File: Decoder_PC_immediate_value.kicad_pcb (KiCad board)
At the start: 4 copper layers, 66.4 x 62.6 mm, 10 parts

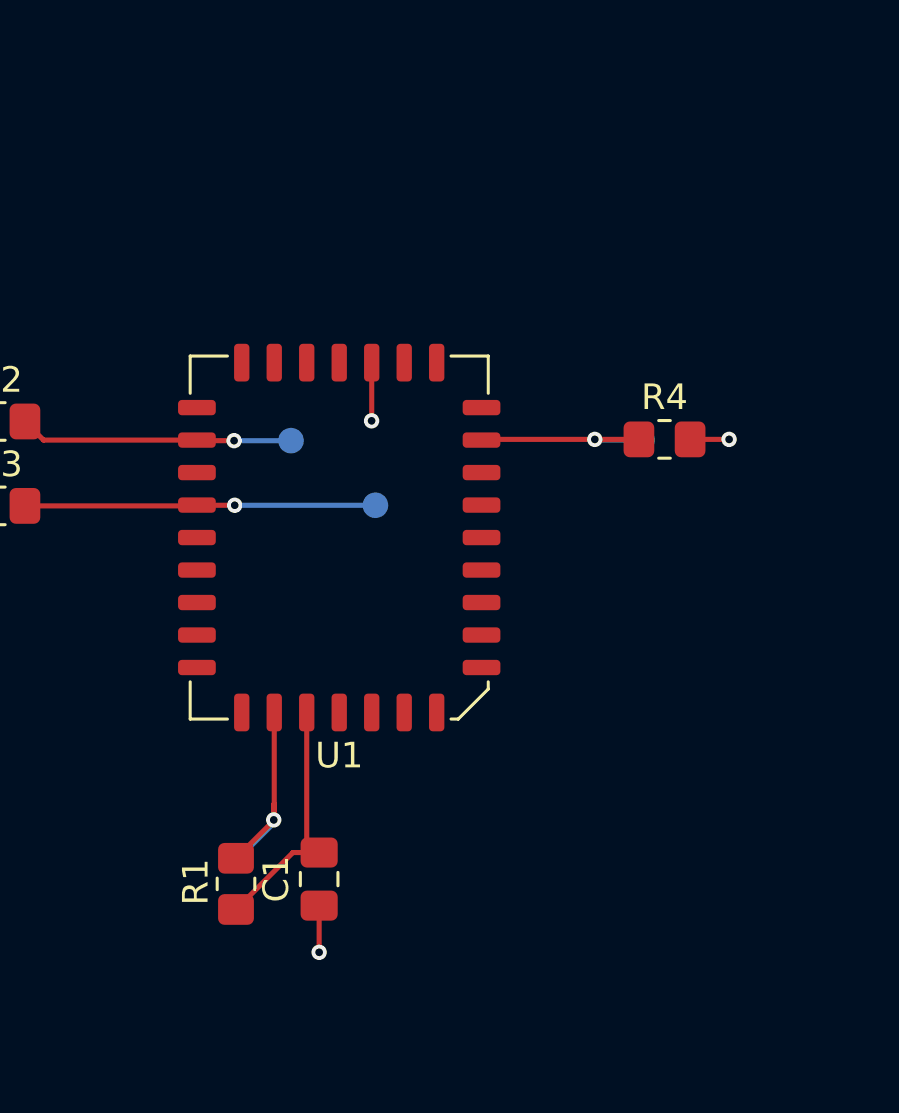
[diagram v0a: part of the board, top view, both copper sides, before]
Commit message: Added Output for Control Byte
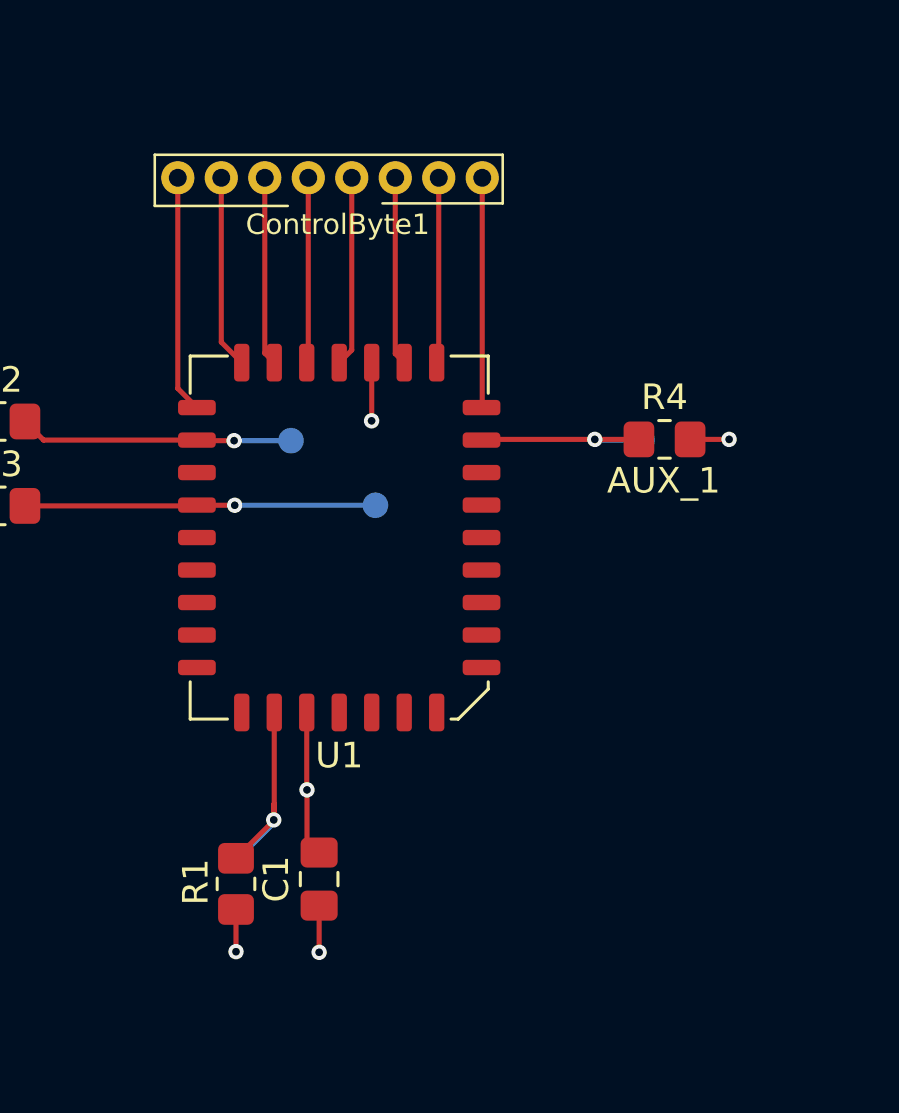
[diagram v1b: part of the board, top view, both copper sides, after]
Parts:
- added ControlByte1: ~, Other:8 Bit Bus Small, F.Cu at (94.5, 61.1)
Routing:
- net ControlWord7: track 0.00 -> 9.29 mm
- net ControlWord0: track 0.00 -> 8.99 mm
- net ControlWord6: track 0.00 -> 7.56 mm
- net ControlWord3: track 0.00 -> 7.43 mm
- net ControlWord5: track 0.00 -> 7.38 mm
- net ControlWord2: track 0.00 -> 7.37 mm
- net ControlWord1: track 0.00 -> 7.26 mm
- net ControlWord4: track 0.00 -> 7.25 mm
- net VCC: track 9.85 -> 8.01 mm, vias 0 -> 2
- added copper zone on In1.Cu, net VCC
- removed copper zone on In1.Cu, net (none)
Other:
- board text added: "AUX_1"

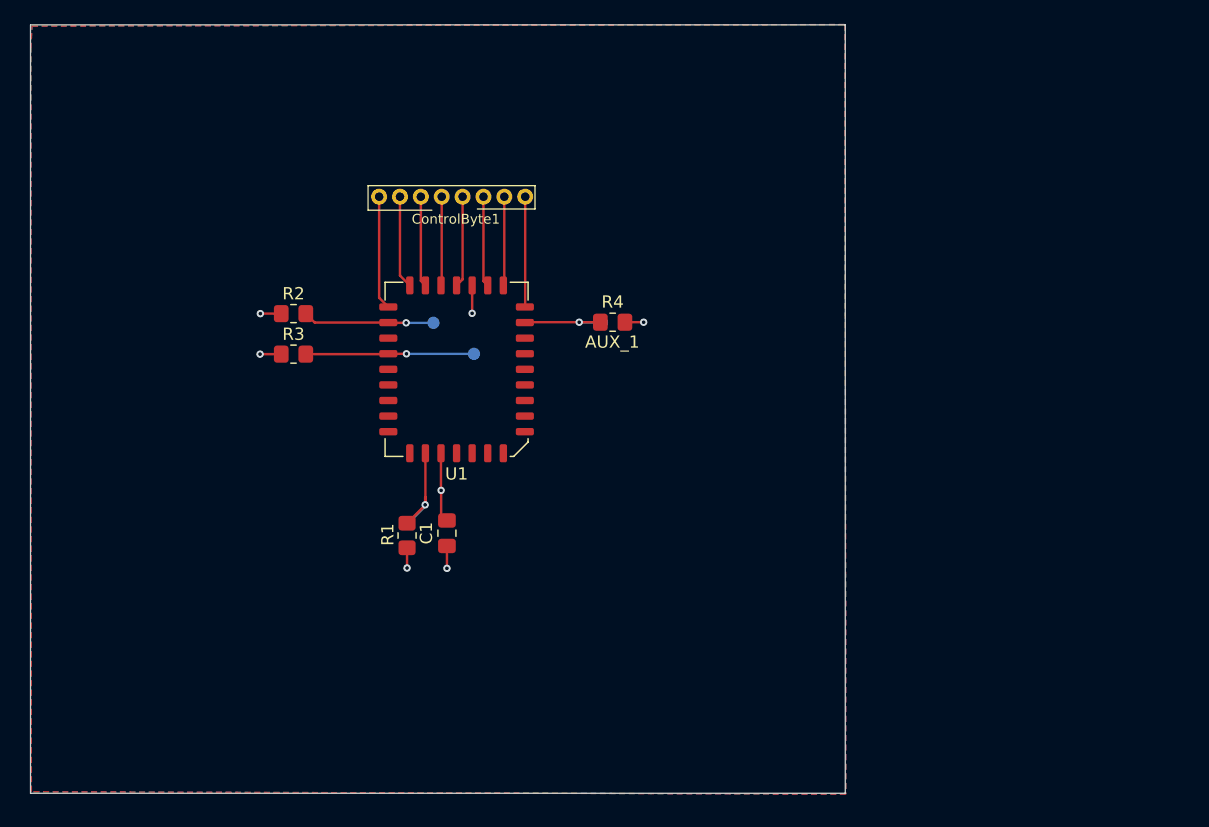
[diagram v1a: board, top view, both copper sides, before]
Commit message: Added Inputs for OP-Code
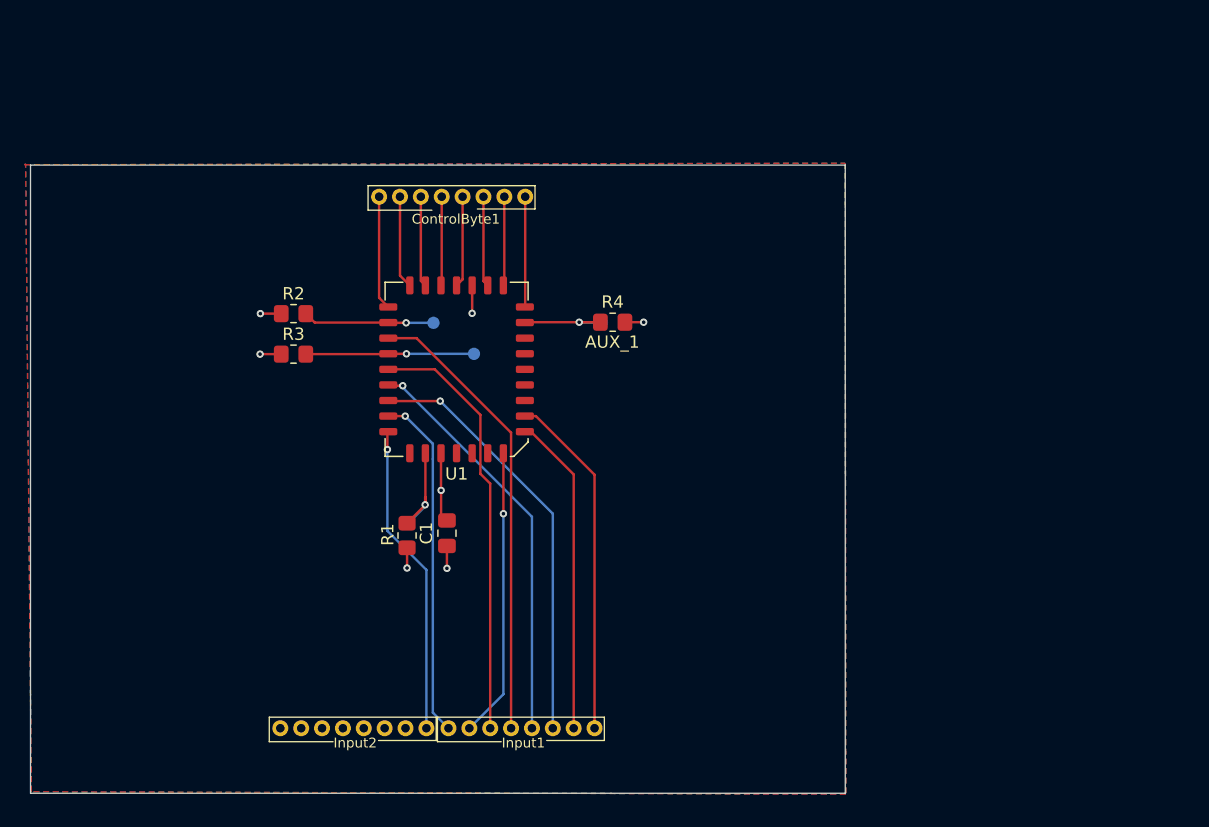
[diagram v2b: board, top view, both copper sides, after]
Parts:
- added Input1: ~, Other:8 Bit Bus Small, F.Cu at (100.2, 104.4)
- added Input2: ~, Other:8 Bit Bus Small, F.Cu at (86.5, 104.4)
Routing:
- net OP_Code_5: track 0.00 -> 37.3 mm
- net OP_Code_6: track 0.00 -> 34.9 mm
- net OP_Code_3: track 0.00 -> 34.7 mm, vias 0 -> 1
- net OP_Code_4: track 0.00 -> 33.5 mm, vias 0 -> 1
- net OP_Code_1: track 0.00 -> 28.3 mm
- net OP_Code_8: track 0.00 -> 28.3 mm, vias 0 -> 1
- net OP_Code_2: track 0.00 -> 26.1 mm
- net OP_Code_9: track 0.00 -> 25.5 mm, vias 0 -> 1
- net OP_Code_7: track 0.00 -> 23.6 mm, vias 0 -> 1
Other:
- board size 66.4 x 62.6 mm -> 66.4 x 51.2 mm

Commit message: Finished Decoder Design
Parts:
- removed R4: 330Ω, Resistor_SMD:R_0805_2012Metric_Pad1.20x1.40mm_HandSolder
- removed TP4: AUX1, TestPoint:TestPoint_Pad_D1.0mm
- moved Input2 14.3 mm to (100.8, 105.2)
- moved Input1 13.1 mm to (87.0, 105.2)
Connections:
- Input2 pad 1: OP_Code_9 -> PM
- Input2 pad 2: unconnected-(Input2-Pad2) -> ZF
- Input2 pad 3: unconnected-(Input2-Pad3) -> Stage_5
- Input2 pad 4: unconnected-(Input2-Pad4) -> Stage_4
- Input2 pad 5: unconnected-(Input2-Pad5) -> Stage_3
- Input2 pad 6: unconnected-(Input2-Pad6) -> Stage_2
- Input2 pad 7: unconnected-(Input2-Pad7) -> Stage_1
- Input2 pad 8: unconnected-(Input2-Pad8) -> OP_Code_9
- U1 pad 12: AUX_1 -> /CLK
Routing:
- net Stage_1: track 0.00 -> 35.2 mm, vias 0 -> 3
- net Stage_2: track 0.00 -> 32.9 mm, vias 0 -> 2
- net Stage_3: track 0.00 -> 31.2 mm, vias 0 -> 2
- net Stage_4: track 0.00 -> 29.7 mm, vias 0 -> 2
- net Stage_5: track 0.00 -> 29.6 mm
- net PM: track 0.00 -> 27.7 mm, vias 0 -> 2
- net ZF: track 0.00 -> 26.3 mm, vias 0 -> 2
- net AUX_1: track 8.02 -> 0.00 mm, vias 1 -> 0
- net OP_Code_7: track 23.6 -> 29.8 mm
- net OP_Code_3: track 34.7 -> 28.6 mm, vias 1 -> 0
- net OP_Code_8: track 28.3 -> 32.9 mm, vias 1 -> 0
- net OP_Code_1: track 28.3 -> 32.3 mm
- net OP_Code_4: track 33.5 -> 29.8 mm, vias 1 -> 2
- net OP_Code_2: track 26.1 -> 29.2 mm
- net OP_Code_5: track 37.3 -> 34.9 mm, vias 0 -> 2
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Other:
- board text added: "1"
- board text added: "5"
- board text added: "8"
- board text added: "9"
- board text added: "OP-Code"
- board text added: "P"
- board text added: "Stage"
- board text added: "Z"
- board text removed: "AUX1"
- board text removed: "AUX_1"

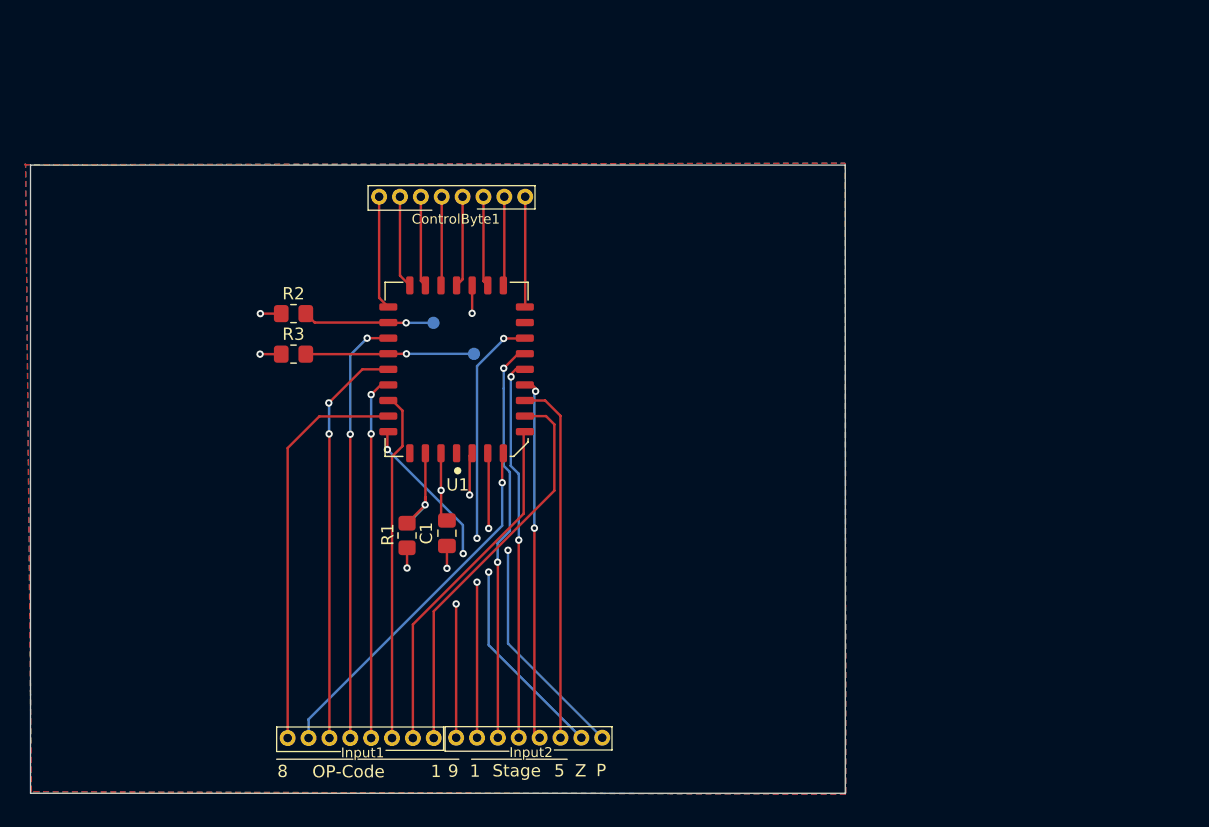
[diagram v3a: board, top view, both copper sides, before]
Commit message: Added Decoder 1/2
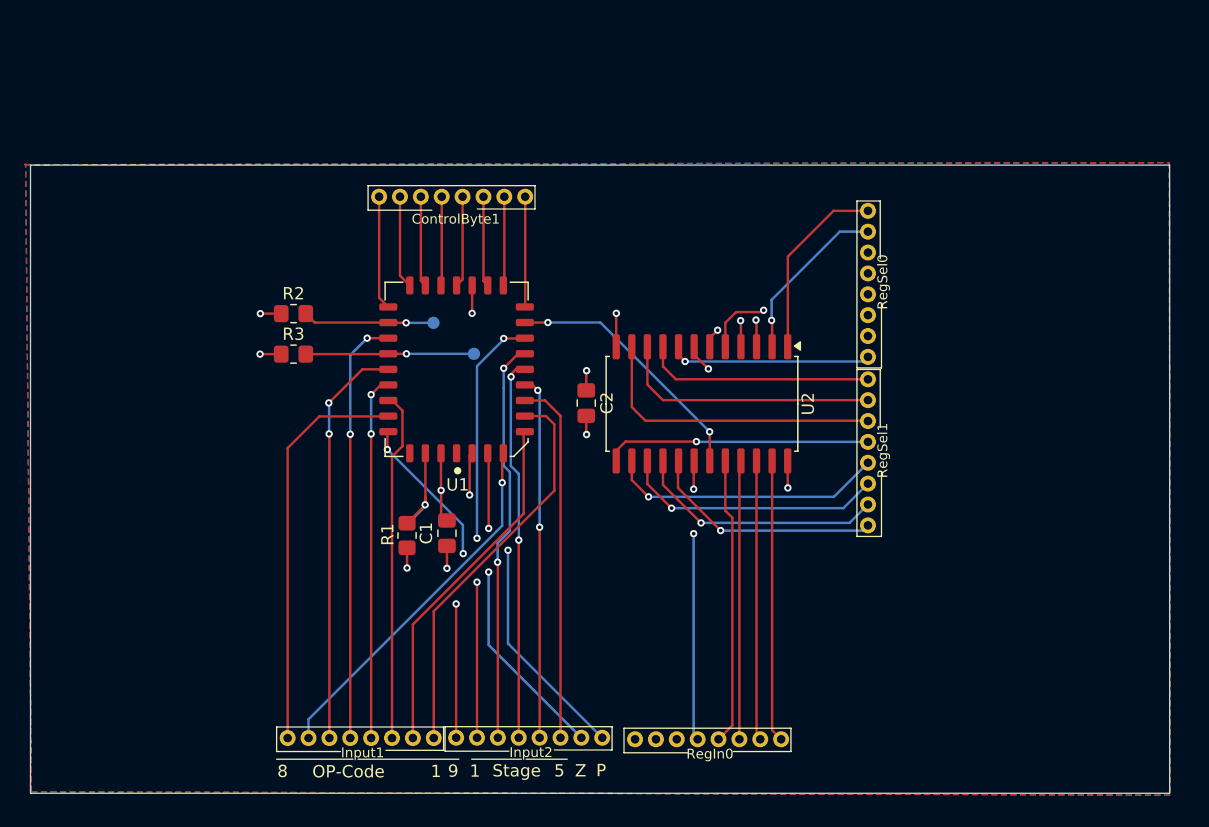
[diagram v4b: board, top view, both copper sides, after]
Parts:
- added C2: 0.1µF, Capacitor_SMD:C_0805_2012Metric_Pad1.18x1.45mm_HandSolder, F.Cu at (105.3, 77.9)
- added RegIn0: ~, Other:8 Bit Bus Small, F.Cu at (115.3, 105.3)
- added RegSel0: ~, Other:8 Bit Bus Small, F.Cu at (128.2, 68.0)
- added RegSel1: ~, Other:8 Bit Bus Small, F.Cu at (128.2, 81.8)
- added U2: ~, Package_SO:SOIC-24W_7.5x15.4mm_P1.27mm, F.Cu at (114.7, 78.0)
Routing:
- net Net-(U2-Y10): track 0.00 -> 24.6 mm
- net REG3: track 0.00 -> 23.4 mm
- net REG0: track 0.00 -> 23.1 mm
- net REG4: track 0.00 -> 22.8 mm, vias 0 -> 2
- net REG1: track 0.00 -> 22.8 mm
- net REG2: track 0.00 -> 22.7 mm
- net Net-(U2-Y12): track 0.00 -> 22.5 mm, vias 0 -> 1
- net Net-(U2-Y11): track 0.00 -> 21.7 mm, vias 0 -> 1
- net Net-(U2-Y9): track 0.00 -> 21.6 mm
- net Net-(U2-Y13): track 0.00 -> 21.5 mm, vias 0 -> 1
- net /CLK: track 0.04 -> 21.2 mm, vias 0 -> 2
- net Net-(U2-Y14): track 0.00 -> 20.6 mm, vias 0 -> 1
- net Net-(U2-Y15): track 0.00 -> 19.3 mm, vias 0 -> 1
- net Net-(U2-Y8): track 0.00 -> 18.7 mm
- net Net-(U2-Y7): track 0.00 -> 16.5 mm, vias 0 -> 1
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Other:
- board size 66.4 x 51.2 mm -> 92.8 x 51.2 mm

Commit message: Added Second Decoder
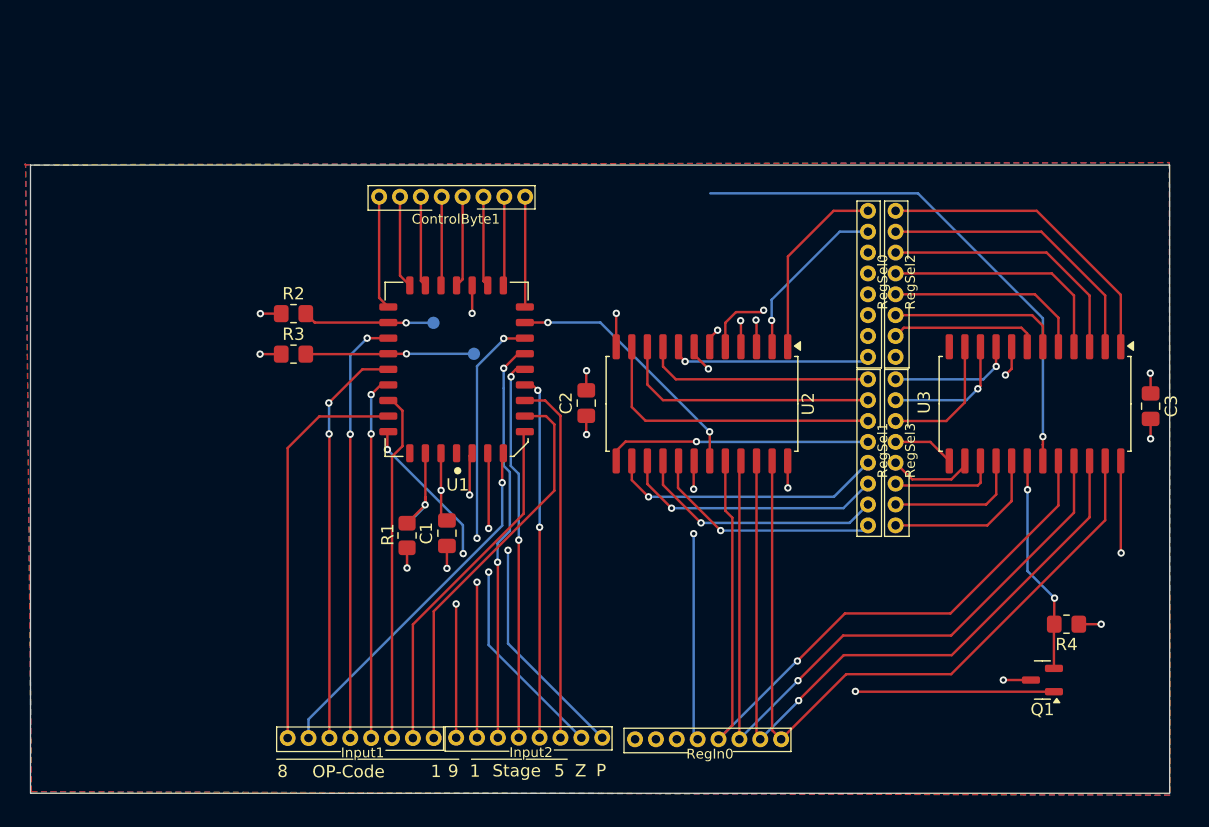
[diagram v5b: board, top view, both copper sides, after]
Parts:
- added C3: 0.1µF, Capacitor_SMD:C_0805_2012Metric_Pad1.18x1.45mm_HandSolder, F.Cu at (151.2, 78.2)
- added Q1: BC818, Package_TO_SOT_SMD:SOT-23, F.Cu at (142.4, 100.5)
- added R4: 300Ω, Resistor_SMD:R_0805_2012Metric_Pad1.20x1.40mm_HandSolder, F.Cu at (144.4, 95.9)
- added RegSel2: ~, Other:8 Bit Bus Small, F.Cu at (130.5, 68.0)
- added RegSel3: ~, Other:8 Bit Bus Small, F.Cu at (130.5, 81.8)
- added U3: ~, Package_SO:SOIC-24W_7.5x15.4mm_P1.27mm, F.Cu at (141.8, 78.0)
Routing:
- net /CLK: track 21.2 -> 64.1 mm, vias 2 -> 3
- net REG3: track 23.4 -> 62.6 mm, vias 0 -> 1
- net REG2: track 22.7 -> 61.8 mm, vias 0 -> 1
- net REG1: track 22.8 -> 61.7 mm, vias 0 -> 1
- net REG0: track 23.1 -> 61.7 mm
- net REG4: track 22.8 -> 53.8 mm, vias 2 -> 3
- net Net-(U3-Y0): track 0.00 -> 25.4 mm
- net Net-(U3-Y1): track 0.00 -> 23.4 mm
- net Net-(U3-Y2): track 0.00 -> 21.4 mm
- net Net-(U3-Y3): track 0.00 -> 19.4 mm
- net /REG4: track 0.00 -> 17.8 mm, vias 0 -> 2
- net Net-(U3-Y4): track 0.00 -> 16.4 mm
- net Net-(U3-Y5): track 0.00 -> 14.1 mm
- net Net-(U3-Y15): track 0.00 -> 13.5 mm
- net Net-(U3-Y6): track 0.00 -> 12.3 mm
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
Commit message: Added Power Source
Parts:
- added B1: ~, Other:Single Bit Bus, F.Cu at (115.0, 65.7)
- added D1: D, Diode_THT:D_5W_P10.16mm_Horizontal, F.Cu at (76.0, 76.9)
- added U5: ~, Other:Vcc & GND, F.Cu at (108.1, 65.7)
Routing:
- net Net-(D1-A): track 0.00 -> 30.1 mm
- net /CLK: track 64.1 -> 77.4 mm
- net GND: track 15.8 -> 18.4 mm, vias 8 -> 9
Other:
- board size 92.8 x 51.2 mm -> 81.4 x 51.2 mm
- board text added: "/CLK"

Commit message: Corrected Addressing Of Decoders
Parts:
- added R5: 0Ω, Resistor_SMD:R_0805_2012Metric_Pad1.20x1.40mm_HandSolder, F.Cu at (105.2, 61.1)
- added R6: 300Ω, Resistor_SMD:R_0805_2012Metric_Pad1.20x1.40mm_HandSolder, F.Cu at (110.4, 61.1)
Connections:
- U2 pad 19: /CLK -> /REG_ACT
- U3 pad 19: /CLK -> /REG_ACT
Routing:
- net /REG_ACT: track 0.00 -> 79.3 mm, vias 0 -> 4
- net /CLK: track 77.4 -> 17.1 mm, vias 3 -> 1
- net ControlWord0: track 8.99 -> 12.9 mm
- net VCC: track 22.7 -> 24.8 mm, vias 7 -> 8
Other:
- outline, holes or cut-outs redrawn
